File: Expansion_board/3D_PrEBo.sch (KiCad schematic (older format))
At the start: 69 parts, among them J1 LED, J10 FAN&LED_INPUT, J11 TMC_INPUT, J12 Fan_interconnection_header, J13 Conn_01x04, J14 Conn_01x03, J2 RJ45, J3 X, J4 Y, J5 Z, J6 E0, J7 E1, J9 X_endstop, M1 Fan_3pin, M2 Fan_3pin, M3 Fan_3pin, M4 Fan_3pin, M5 Fan_3pin, M6 Fan_3pin, M7 Fan_3pin, M8 Fan_4pin, Q1 AOD4189, Q10 IRLML2502, Q2 IRLML2502, Q3 IRLML2502, Q4 IRLML2502, Q5 IRLML2502, Q6 IRLML2502, Q7 IRLML2502, Q8 IRLML2502, Q9 IRLML2502, U1 L5973D, U2 NCP1117-5.0_SOT223

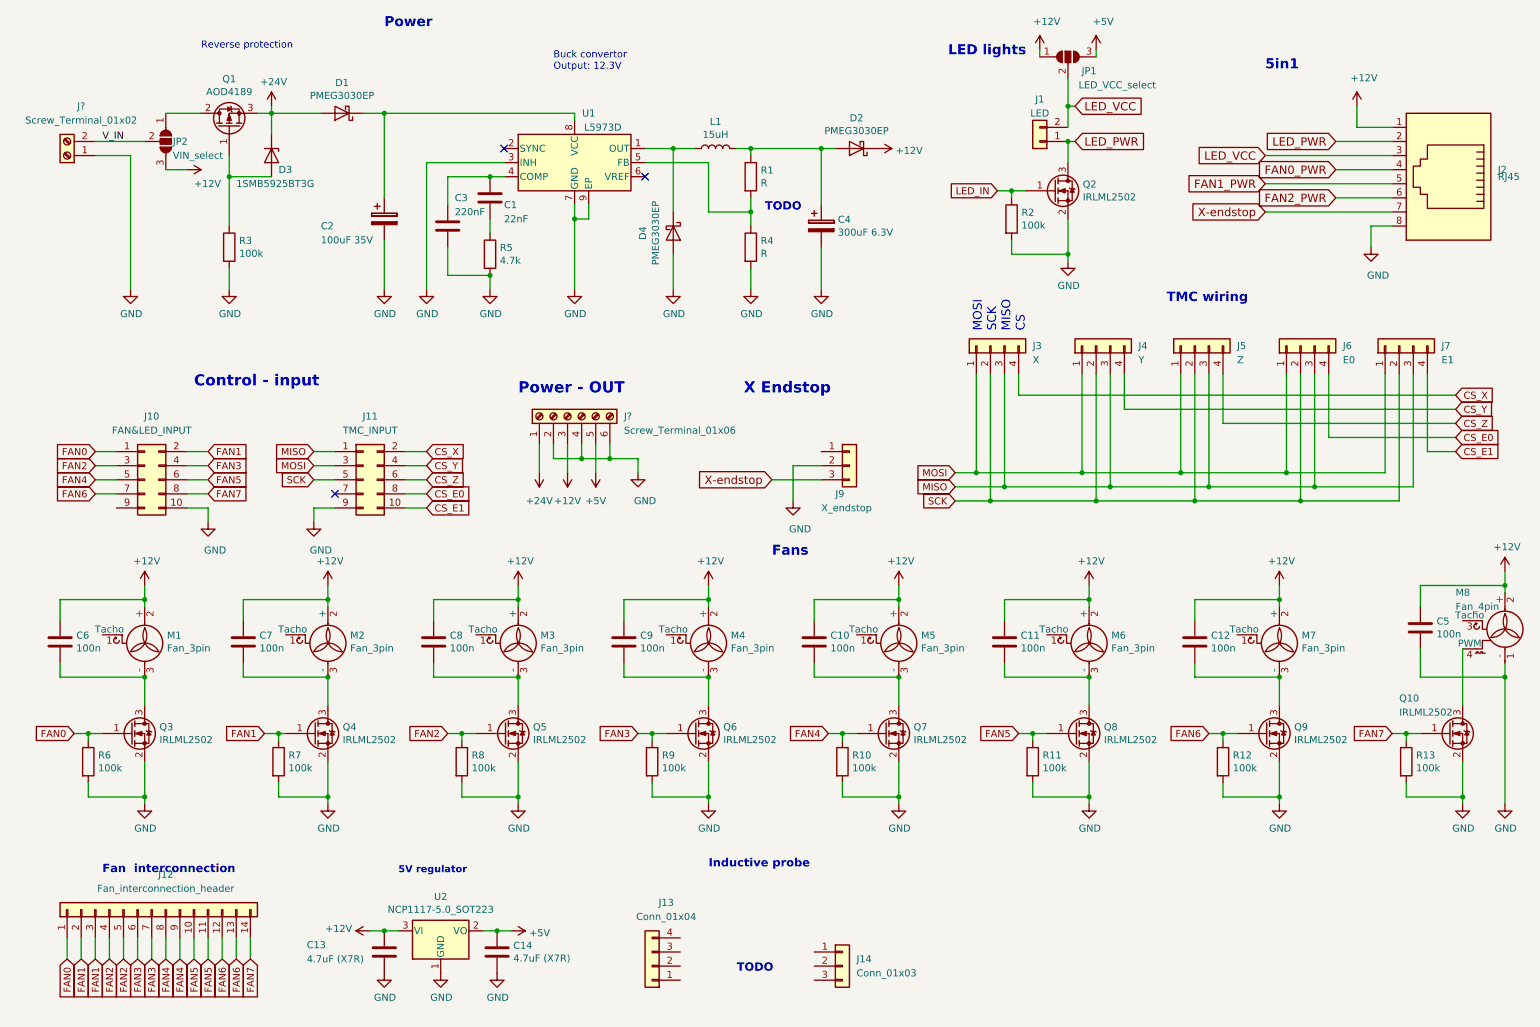
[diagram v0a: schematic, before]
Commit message: Schematic: Add schematic in pdf, minor part shifting in schema
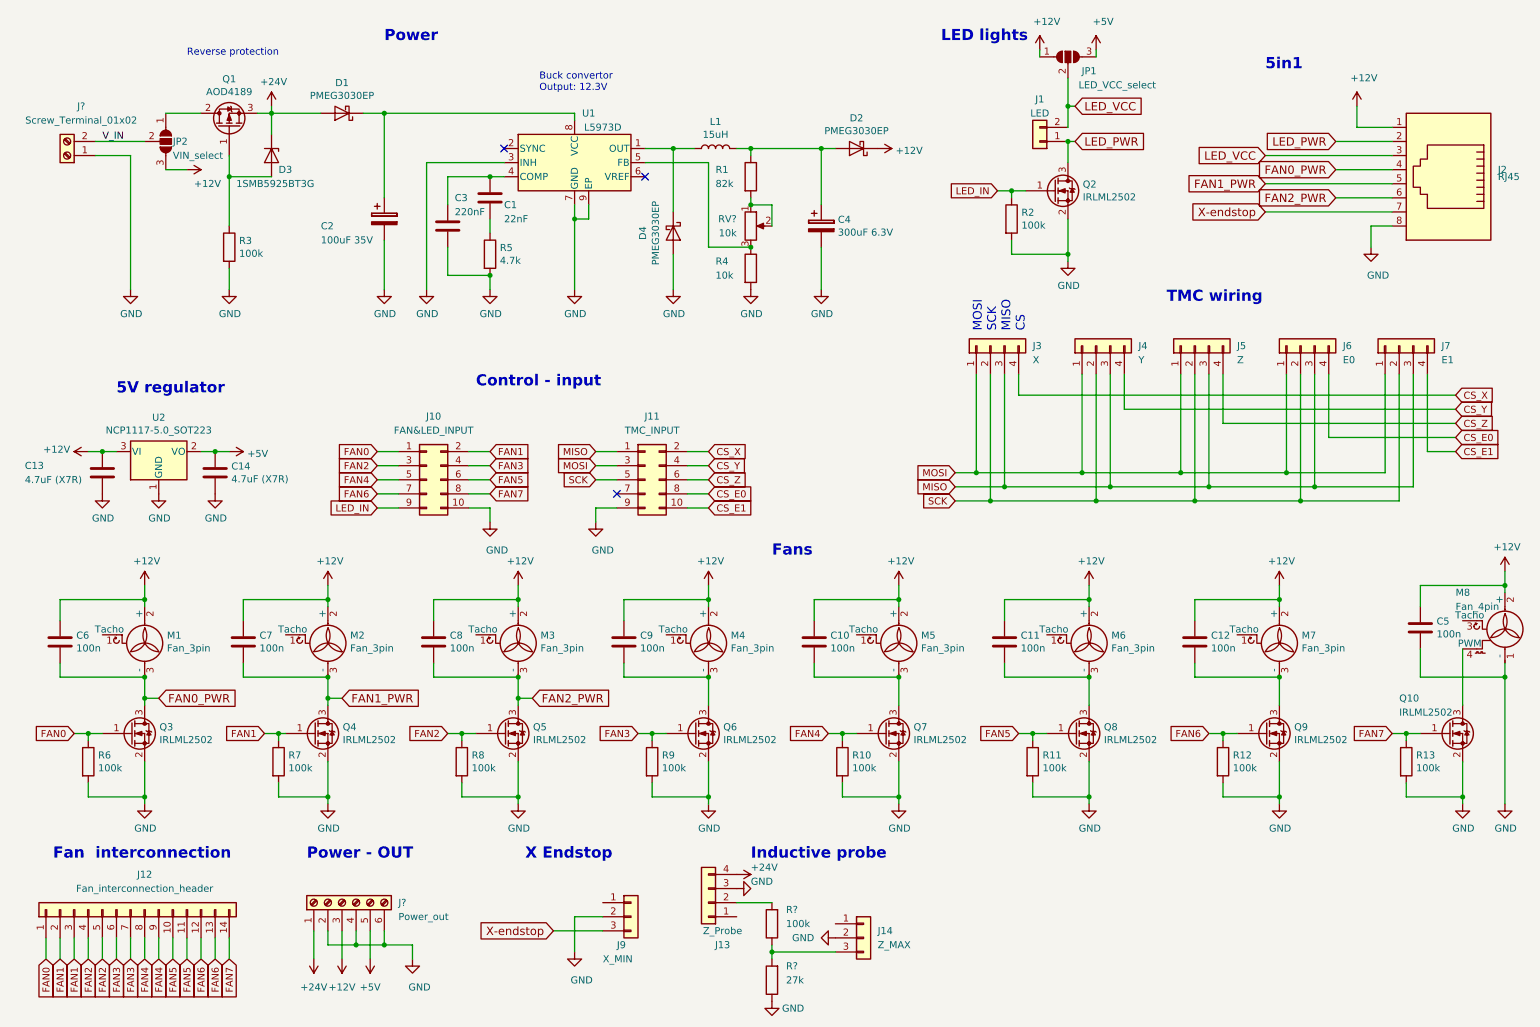
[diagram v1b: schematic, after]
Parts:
- added R?: 100k, symbol Device:R
- added R?: 27k, symbol Device:R
- added RV?: 10k, symbol Device:R_POT
- J13: value Conn_01x04 -> Z_Probe
- J14: value Conn_01x03 -> Z_MAX
- J9: value X_endstop -> X_MIN
- J?: value Screw_Terminal_01x06 -> Power_out
- R1: value R -> 82k
- R4: value R -> 10k
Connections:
- net +24V: now also J13.4 (Pin_4)
- net FAN0_PWR: now also C6.2, M1.3 (-), Q3.3 (D)
- net FAN1_PWR: now also C7.2, M2.3 (-), Q4.3 (D)
- net FAN2_PWR: now also C8.2, M3.3 (-), Q5.3 (D)
- net GND: now also J13.3 (Pin_3), J14.2 (Pin_2), R?.1
- net LED_IN: now also J10.9 (Pin_9)
- net at R4.1, U1.5 (FB): now also RV?.3; no longer R1.2
- net at J13.2 (Pin_2): now also R?.2
- net at J14.3 (Pin_3): now also R?.1, R?.2
- new net: R1.2, RV?.1, RV?.2
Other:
- note added: "Inductive probe"
- note removed: "Inductive probe\n\n\n"
- note removed: "TODO"
- moved on the sheet: C13, C14, J10, J11, J12, J13, J14, J9, J?, R4, U2

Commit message: Schema: Update part labels, Rewrite project description
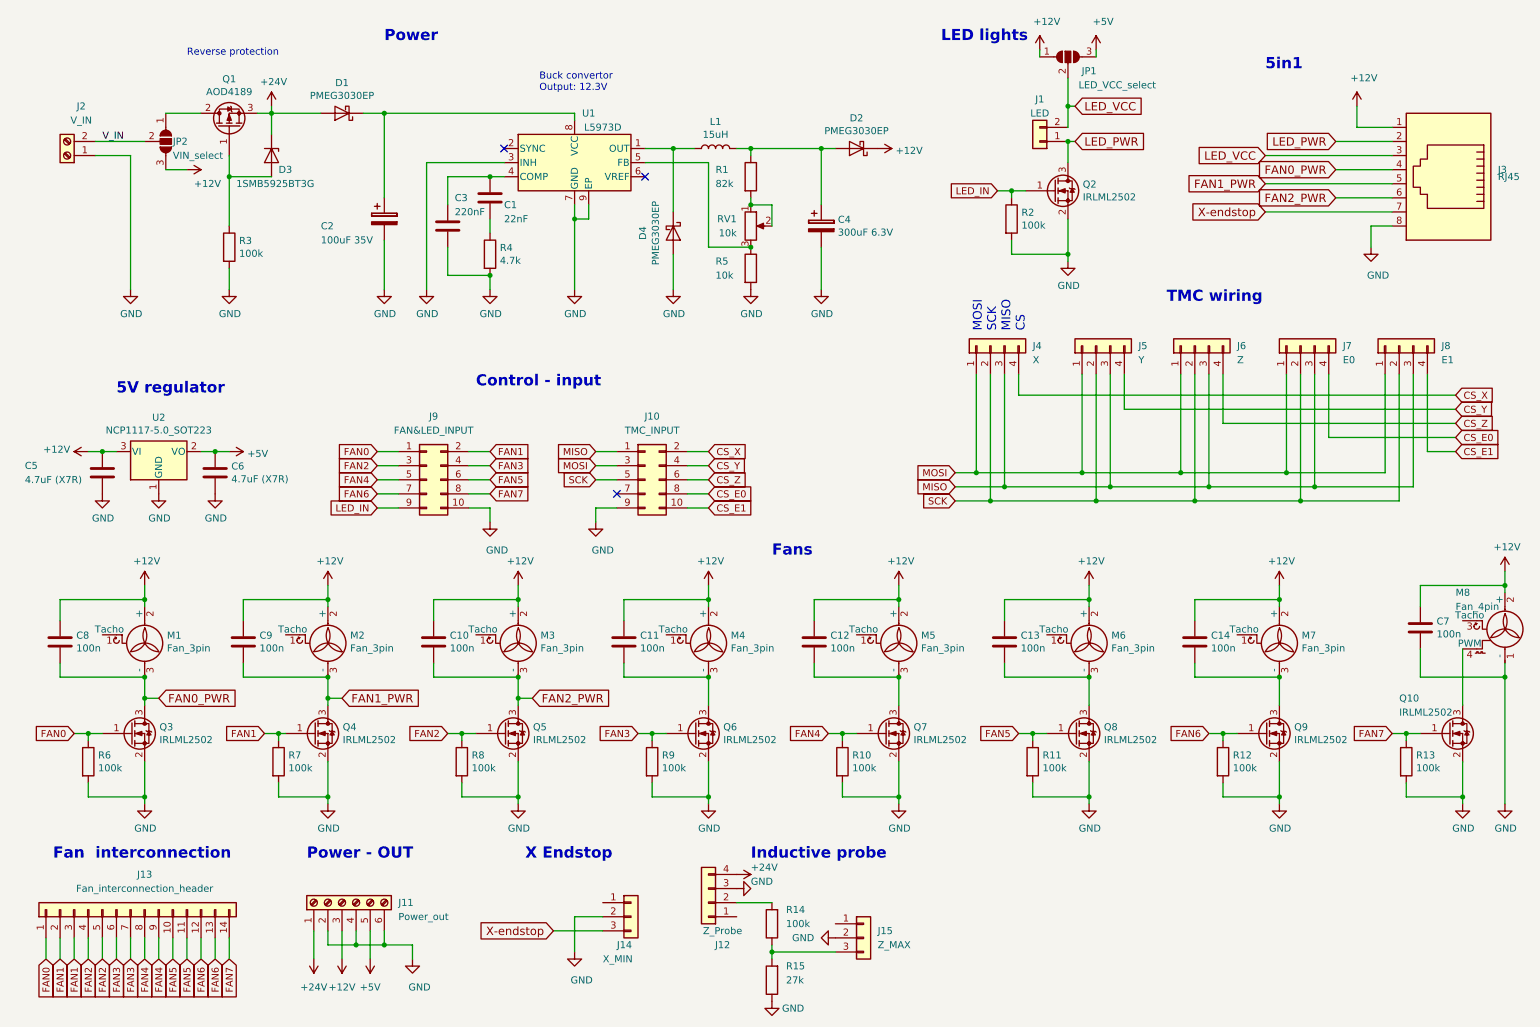
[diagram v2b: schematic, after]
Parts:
- C10: renamed from C8; footprint (none) -> Capacitor_SMD:C_0603_1608Metric
- C11: renamed from C9; footprint (none) -> Capacitor_SMD:C_0603_1608Metric
- C12: renamed from C10; footprint (none) -> Capacitor_SMD:C_0603_1608Metric
- C13: renamed from C11; footprint (none) -> Capacitor_SMD:C_0603_1608Metric
- C14: renamed from C12; footprint (none) -> Capacitor_SMD:C_0603_1608Metric
- C7: renamed from C5; footprint (none) -> Capacitor_SMD:C_0603_1608Metric
- C8: renamed from C6; footprint (none) -> Capacitor_SMD:C_0603_1608Metric
- C9: renamed from C7; footprint (none) -> Capacitor_SMD:C_0603_1608Metric
- J1: footprint (none) -> Connector_JST:JST_XH_S02B-XH-A-1_1x02_P2.50mm_Horizontal
- J10: renamed from J11; footprint (none) -> Connector_IDC:IDC-Header_2x05_P2.54mm_Horizontal
- J11: renamed from J?; footprint (none) -> TerminalBlock_Phoenix:TerminalBlock_Phoenix_MKDS-1,5-6_1x06_P5.00mm_Horizontal
- J12: renamed from J13; footprint (none) -> Connector:FanPinHeader_1x04_P2.54mm_Vertical
- J13: renamed from J12; footprint (none) -> Connector_PinHeader_2.54mm:PinHeader_1x14_P2.54mm_Vertical
- J14: renamed from J9; footprint (none) -> Connector_JST:JST_XH_S03B-XH-A-1_1x03_P2.50mm_Horizontal
- J15: renamed from J14; footprint (none) -> Connector_JST:JST_XH_S03B-XH-A-1_1x03_P2.50mm_Horizontal
- J2: renamed from J?; value Screw_Terminal_01x02 -> V_IN; footprint (none) -> TerminalBlock_Phoenix:TerminalBlock_Phoenix_MKDS-1,5-2_1x02_P5.00mm_Horizontal
- J3: renamed from J2; footprint (none) -> Connector_RJ:RJ45_Amphenol_54602-x08_Horizontal
- J4: renamed from J3; footprint (none) -> Connector_PinHeader_2.54mm:PinHeader_1x04_P2.54mm_Horizontal
- J5: renamed from J4; footprint (none) -> Connector_PinHeader_2.54mm:PinHeader_1x04_P2.54mm_Horizontal
- J6: renamed from J5; footprint (none) -> Connector_PinHeader_2.54mm:PinHeader_1x04_P2.54mm_Horizontal
- J7: renamed from J6; footprint (none) -> Connector_PinHeader_2.54mm:PinHeader_1x04_P2.54mm_Horizontal
- J8: renamed from J7; footprint (none) -> Connector_PinHeader_2.54mm:PinHeader_1x04_P2.54mm_Horizontal
- J9: renamed from J10; footprint (none) -> Connector_IDC:IDC-Header_2x05_P2.54mm_Horizontal
- JP1, JP2: footprint (none) -> Jumper:SolderJumper-3_P1.3mm_Open_RoundedPad1.0x1.5mm
- M1, M2, M3, M4, M5, M6, M7: footprint (none) -> Connector:FanPinHeader_1x03_P2.54mm_Vertical
- M8: footprint (none) -> Connector:FanPinHeader_1x04_P2.54mm_Vertical
- Q10, Q2, Q3, Q4, Q5, Q6, Q7, Q8, Q9: footprint (none) -> Package_TO_SOT_SMD:TSOT-23
- R10, R11, R12, R13, R2, R6, R7, R8, R9: footprint (none) -> Resistor_SMD:R_0603_1608Metric
- R14, R15: renamed from R?; footprint (none) -> Resistor_SMD:R_0603_1608Metric
- gave numbers to parts that had none: 1
- renumbered C13 to C5, C14 to C6, R5 to R4, R4 to R5

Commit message: Expansion_board: PCB: Add PCB outlines, position some parts on PCB
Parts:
- RV1: footprint (none) -> Potentiometer_SMD:Potentiometer_Bourns_3214J_Horizontal
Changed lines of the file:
@@
 EESchema Schematic File Version 4
+LIBS:3D_PrEBo-cache
 EELAYER 26 0
 EELAYER END
@@
 F 0 "RV1" H 5550 2150 50  0000 R CNN
 F 1 "10k" H 5550 2050 50  0000 R CNN
-F 2 "" H 5650 2100 50  0001 C CNN
+F 2 "Potentiometer_SMD:Potentiometer_Bourns_3214J_Horizontal" H 5650 2100 50  0001 C CNN
 F 3 "~" H 5650 2100 50  0001 C CNN
 	1    5650 2100

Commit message: Expansion_board: PCB: Place all parts, routing of voltage regulator
Change horizontal fan connector to vertical.
Pour cooper planes on both sides.
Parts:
- J1: footprint Connector_JST:JST_XH_S02B-XH-A-1_1x02_P2.50mm_Horizontal -> Connector_JST:JST_XH_B02B-XH-A_1x02_P2.50mm_Vertical
- J12: footprint Connector:FanPinHeader_1x04_P2.54mm_Vertical -> Connector_JST:JST_XH_B04B-XH-A_1x04_P2.50mm_Vertical
- M1, M2, M3, M4, M5, M6, M7: footprint Connector:FanPinHeader_1x03_P2.54mm_Vertical -> Connector_JST:JST_XH_S03B-XH-A_1x03_P2.50mm_Horizontal
- M8: footprint Connector:FanPinHeader_1x04_P2.54mm_Vertical -> Connector_JST:JST_XH_S04B-XH-A_1x04_P2.50mm_Horizontal
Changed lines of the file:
@@
 F 0 "M1" H 1508 4996 50  0000 L CNN
 F 1 "Fan_3pin" H 1508 4905 50  0000 L CNN
-F 2 "Connector:FanPinHeader_1x03_P2.54mm_Vertical" H 1350 4910 50  0001 C CNN
+F 2 "Connector_JST:JST_XH_S03B-XH-A_1x03_P2.50mm_Horizontal" H 1350 4910 50  0001 C CNN
 F 3 "http://www.hardwarecanucks.com/forum/attachments/new-builds/16287d1330775095-help-chassis-power-fan-connectors-motherboard-asus_p8z68.jpg" H 1350 4910 50  0001 C CNN
 	1    1350 5000
@@
 F 0 "M2" H 2808 4996 50  0000 L CNN
 F 1 "Fan_3pin" H 2808 4905 50  0000 L CNN
-F 2 "Connector:FanPinHeader_1x03_P2.54mm_Vertical" H 2650 4910 50  0001 C CNN
+F 2 "Connector_JST:JST_XH_S03B-XH-A_1x03_P2.50mm_Horizontal" H 2650 4910 50  0001 C CNN
 F 3 "http://www.hardwarecanucks.com/forum/attachments/new-builds/16287d1330775095-help-chassis-power-fan-connectors-motherboard-asus_p8z68.jpg" H 2650 4910 50  0001 C CNN
 	1    2650 5000
@@
 F 0 "M3" H 4158 4996 50  0000 L CNN
 F 1 "Fan_3pin" H 4158 4905 50  0000 L CNN
-F 2 "Connector:FanPinHeader_1x03_P2.54mm_Vertical" H 4000 4910 50  0001 C CNN
+F 2 "Connector_JST:JST_XH_S03B-XH-A_1x03_P2.50mm_Horizontal" H 4000 4910 50  0001 C CNN
 F 3 "http://www.hardwarecanucks.com/forum/attachments/new-builds/16287d1330775095-help-chassis-power-fan-connectors-motherboard-asus_p8z68.jpg" H 4000 4910 50  0001 C CNN
 	1    4000 5000
@@
 F 0 "M4" H 5508 4996 50  0000 L CNN
 F 1 "Fan_3pin" H 5508 4905 50  0000 L CNN
-F 2 "Connector:FanPinHeader_1x03_P2.54mm_Vertical" H 5350 4910 50  0001 C CNN
+F 2 "Connector_JST:JST_XH_S03B-XH-A_1x03_P2.50mm_Horizontal" H 5350 4910 50  0001 C CNN
 F 3 "http://www.hardwarecanucks.com/forum/attachments/new-builds/16287d1330775095-help-chassis-power-fan-connectors-motherboard-asus_p8z68.jpg" H 5350 4910 50  0001 C CNN
 	1    5350 5000
@@
 F 0 "M5" H 6858 4996 50  0000 L CNN
 F 1 "Fan_3pin" H 6858 4905 50  0000 L CNN
-F 2 "Connector:FanPinHeader_1x03_P2.54mm_Vertical" H 6700 4910 50  0001 C CNN
+F 2 "Connector_JST:JST_XH_S03B-XH-A_1x03_P2.50mm_Horizontal" H 6700 4910 50  0001 C CNN
 F 3 "http://www.hardwarecanucks.com/forum/attachments/new-builds/16287d1330775095-help-chassis-power-fan-connectors-motherboard-asus_p8z68.jpg" H 6700 4910 50  0001 C CNN
 	1    6700 5000
@@
 F 0 "M6" H 8208 4996 50  0000 L CNN
 F 1 "Fan_3pin" H 8208 4905 50  0000 L CNN
-F 2 "Connector:FanPinHeader_1x03_P2.54mm_Vertical" H 8050 4910 50  0001 C CNN
+F 2 "Connector_JST:JST_XH_S03B-XH-A_1x03_P2.50mm_Horizontal" H 8050 4910 50  0001 C CNN
 F 3 "http://www.hardwarecanucks.com/forum/attachments/new-builds/16287d1330775095-help-chassis-power-fan-connectors-motherboard-asus_p8z68.jpg" H 8050 4910 50  0001 C CNN
 	1    8050 5000
@@
 F 0 "M7" H 9558 4996 50  0000 L CNN
 F 1 "Fan_3pin" H 9558 4905 50  0000 L CNN
-F 2 "Connector:FanPinHeader_1x03_P2.54mm_Vertical" H 9400 4910 50  0001 C CNN
+F 2 "Connector_JST:JST_XH_S03B-XH-A_1x03_P2.50mm_Horizontal" H 9400 4910 50  0001 C CNN
 F 3 "http://www.hardwarecanucks.com/forum/attachments/new-builds/16287d1330775095-help-chassis-power-fan-connectors-motherboard-asus_p8z68.jpg" H 9400 4910 50  0001 C CNN
 	1    9400 5000
@@
 F 0 "M8" H 10650 5300 50  0000 L CNN
 F 1 "Fan_4pin" H 10650 5200 50  0000 L CNN
-F 2 "Connector:FanPinHeader_1x04_P2.54mm_Vertical" H 11000 5010 50  0001 C CNN
+F 2 "Connector_JST:JST_XH_S04B-XH-A_1x04_P2.50mm_Horizontal" H 11000 5010 50  0001 C CNN
 F 3 "http://www.formfactors.org/developer%5Cspecs%5Crev1_2_public.pdf" H 11000 5010 50  0001 C CNN
 	1    11000 5000
@@
 F 0 "J12" H 5250 7200 50  0000 C CNN
 F 1 "Z_Probe" H 5250 7100 50  0000 C CNN
-F 2 "Connector:FanPinHeader_1x04_P2.54mm_Vertical" H 5350 6900 50  0001 C CNN
+F 2 "Connector_JST:JST_XH_B04B-XH-A_1x04_P2.50mm_Vertical" H 5350 6900 50  0001 C CNN
 F 3 "~" H 5350 6900 50  0001 C CNN
 	1    5350 6900
@@
 F 0 "J1" H 7700 1200 50  0000 C CNN
 F 1 "LED" H 7700 1300 50  0000 C CNN
-F 2 "Connector_JST:JST_XH_S02B-XH-A-1_1x02_P2.50mm_Horizontal" H 7700 1500 50  0001 C CNN
+F 2 "Connector_JST:JST_XH_B02B-XH-A_1x02_P2.50mm_Vertical" H 7700 1500 50  0001 C CNN
 F 3 "~" H 7700 1500 50  0001 C CNN
 	1    7700 1500
